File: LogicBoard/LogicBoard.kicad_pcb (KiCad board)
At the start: 4 copper layers, 80 x 81.5 mm, 54 parts, among them M1 MountingHole_3.5mm, M2 MountingHole_3.5mm, M3 MountingHole_3.5mm, M4 MountingHole_3.5mm, Q1 IRF520N, Q2 IRF520N, Q3 IRF520N, U1 STM32H743VITx, U2 MCP2557FD-xSN, U3 MCP2518FD-xQBB, U4 MCP2557FD-xSN, Y1 830033075, Y2 ABS04W32768KHZ6D2T5, Y3 ECS400936BCKYTR

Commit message: Added version with screw terminals
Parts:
- removed the C8 at (58.5, 96.0)
- added J**: TBC05041GG, TBC05-04-1-G-G:TBC05041GG, F.Cu at (45.0, 66.8)
- added J**: TBC05041GG, TBC05-04-1-G-G:TBC05041GG, F.Cu at (45.0, 80.0)
- added J**: TBC05041GG, TBC05-04-1-G-G:TBC05041GG, F.Cu at (46.0, 114.5)
- added MAIN ENCODERS: TBJ05081GG, TBJ05-08-1-G-G:TBJ05081GG, F.Cu at (57.4, 55.0)
- moved M4 12.5 mm to (44.0, 52.5)
- moved M3 11.5 mm to (116.0, 52.5)
- renumbered C5 to C1, C11 to C12, C5 to C2, C6 to C24
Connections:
- R10 pad 2: (no net) -> BatteryHealth
- R11 pad 2: (no net) -> BatteryHealth
- R12 pad 1: (no net) -> BatteryHealth
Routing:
- net TIM1_CH2: track 0.00 -> 53.2 mm, vias 0 -> 2
- net TIM1_CH1: track 0.00 -> 51.1 mm, vias 0 -> 2
- net I2C4_SDA: track 0.00 -> 48.3 mm, vias 0 -> 1
- net I2C2_SDA: track 0.00 -> 40.2 mm, vias 0 -> 2
- net TIM3_CH3: track 0.00 -> 40.1 mm, vias 0 -> 1
- net I2C2_SCL: track 0.00 -> 39.1 mm, vias 0 -> 2
- net TIM3_CH4: track 0.00 -> 38.0 mm, vias 0 -> 1
- net I2C3_SDA: track 0.00 -> 36.1 mm, vias 0 -> 2
- net TIM1_CH4: track 0.00 -> 36.0 mm
- net I2C4_SCL: track 0.00 -> 34.7 mm, vias 0 -> 1
- net TIM3_CH1: track 0.00 -> 34.7 mm
- net TIM1_CH3: track 0.00 -> 34.4 mm, vias 0 -> 1
- net TIM2_CH2: track 0.00 -> 32.9 mm, vias 0 -> 1
- net TIM3_CH2: track 0.00 -> 32.6 mm
- net I2C3_SCL: track 0.00 -> 32.4 mm, vias 0 -> 2
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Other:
- board size 80 x 81.5 mm -> 80.5 x 95 mm
- board text added: "G"
- board text added: "TIM1"
- board text added: "TIM2"
- board text added: "TIM3 (MOTORS)"

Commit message: Prepared BOM, component placement file and minor changes to PCB
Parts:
- C15: value C_0201_0603Metric -> C_0402; footprint Capacitor_SMD:C_0201_0603Metric -> PCM_4ms_Capacitor:C_0402
- J1: renamed from RPI CONN 
- J7: renamed from MAIN ENCODERS
- J8-STLINK: renamed from STLINK 
- R10, R11, R12: value R_0201_0603Metric -> R_1206_3216Metric; footprint Resistor_SMD:R_0201_0603Metric -> PCM_4ms_Resistor:R_1206_3216Metric
- Y1: value 830033075 -> 7I25000F18UCG
- Y3: value ECS400936BCKYTR -> Q24FA20H00209
- moved R11 6.66 mm to (49.1, 97.5)
- moved R10 6.50 mm to (53.0, 95.0), turned to 90 degrees
- moved R12 6.40 mm to (49.1, 94.5), turned to 0 degrees
- moved C15 0.50 mm to (57.0, 88.5)
- renumbered J** to J2, J** to J3, J** to J4, J** to J5, J** to J6
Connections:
- R11 pad 1: +24V -> BatteryHealth
- R11 pad 2: BatteryHealth -> +24V
- R12 pad 1: BatteryHealth -> GND
- R12 pad 2: GND -> BatteryHealth
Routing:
- net GND: track 90.5 -> 99.9 mm
- net BatteryHealth: track 12.7 -> 19.7 mm
- net +24V: track 49.7 -> 45.7 mm
- net VDDA_Conn: track 5.63 -> 5.04 mm

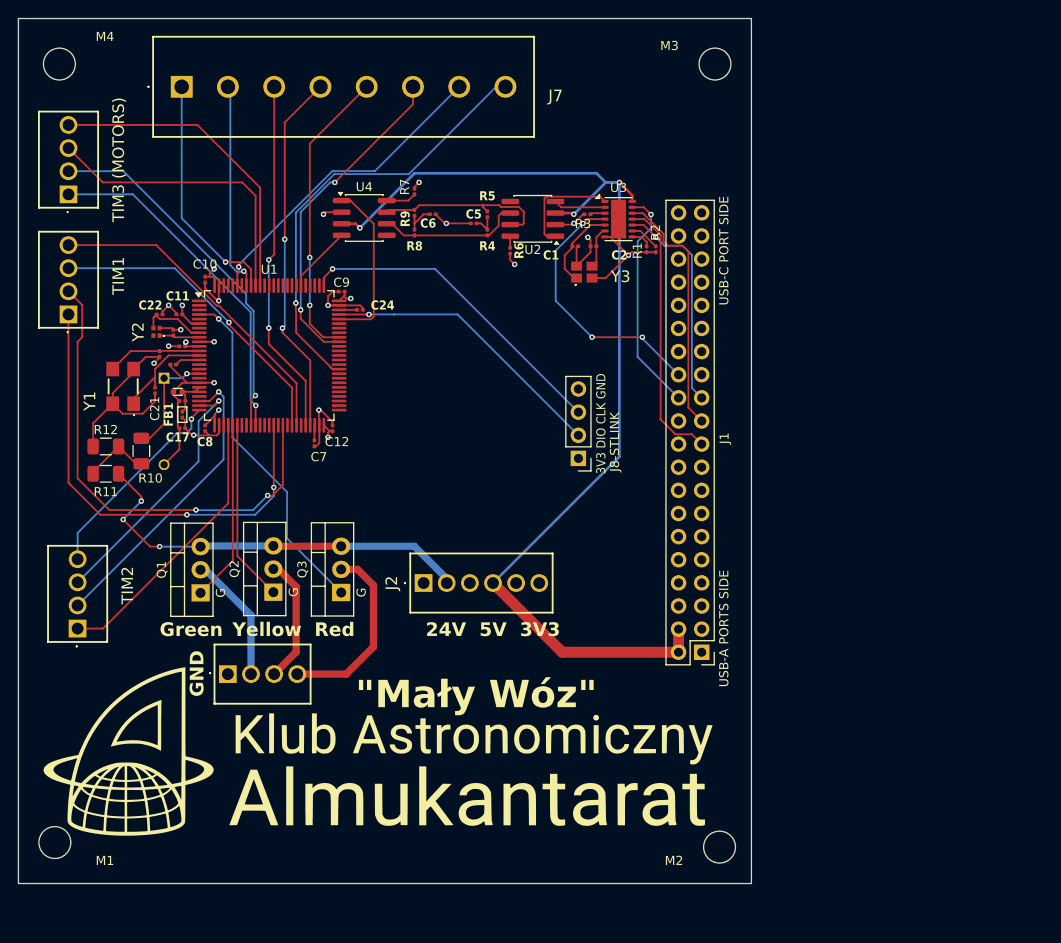
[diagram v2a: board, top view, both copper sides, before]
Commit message: PCB refactor, changed dimensions of passive components and board layout
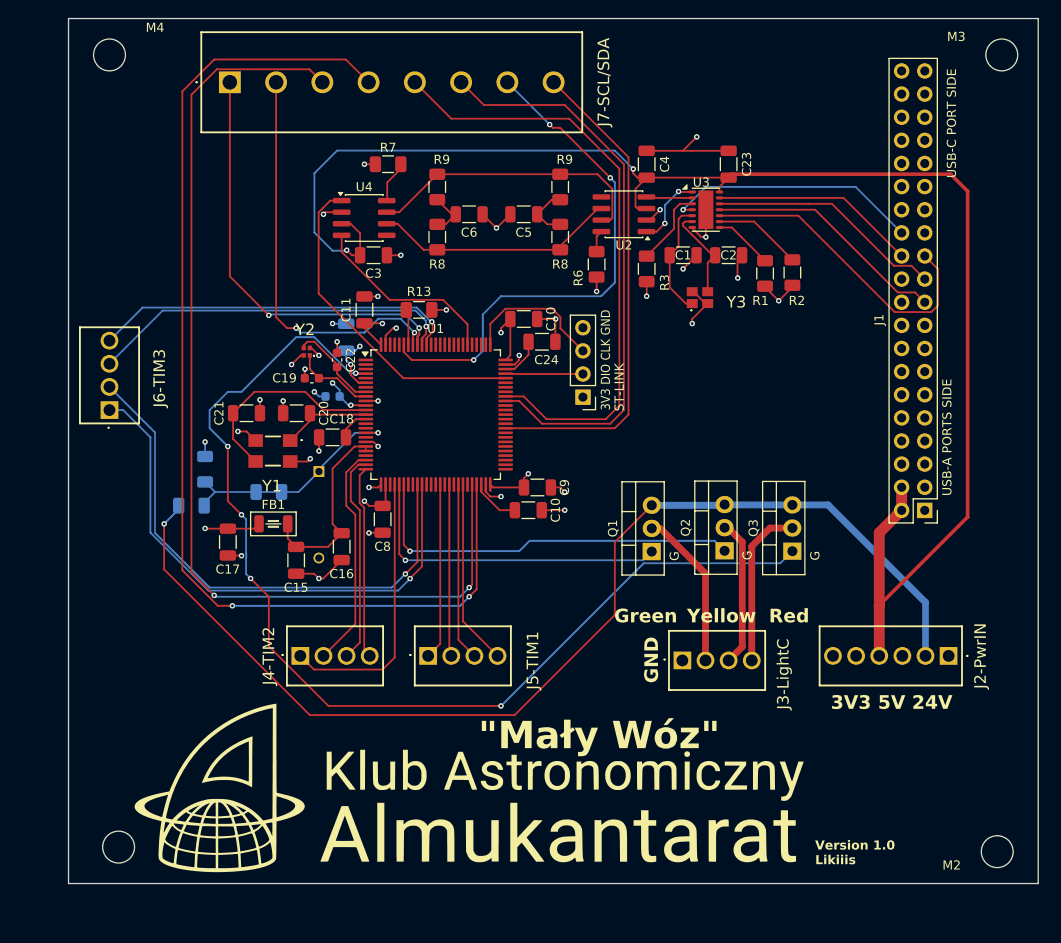
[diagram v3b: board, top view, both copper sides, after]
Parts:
- removed the C10 at (60.0, 76.2)
- removed the C12 at (57.5, 83.5)
- removed the C12 at (74.0, 92.5)
- removed the C21 at (54.5, 88.3)
- removed the C21 at (55.0, 84.3)
- removed C7: C_0201_0603Metric, Capacitor_SMD:C_0201_0603Metric
- removed R4, R5: R_0201_0603Metric, Resistor_SMD:R_0201_0603Metric
- removed the R8 at (83.0, 71.0)
- removed the R9 at (83.0, 68.8)
- added C10: C_1206_3216Metric, Capacitor_SMD:C_1206_3216Metric, F.Cu at (95.0, 80.5)
- added C10: C_1206_3216Metric, Capacitor_SMD:C_1206_3216Metric, F.Cu at (95.5, 101.5)
- added C12: C_1206_3216Metric, Capacitor_SMD:C_1206_3216Metric, B.Cu at (75.5, 82.5)
- added C13: C_0603_1608Metric, Capacitor_SMD:C_0603_1608Metric, B.Cu at (74.0, 89.0)
- added C20: C_1206_3216Metric, Capacitor_SMD:C_1206_3216Metric, F.Cu at (70.0, 90.8)
- added C21: C_1206_3216Metric, Capacitor_SMD:C_1206_3216Metric, F.Cu at (64.5, 90.8)
- added C23: C_1206_3216Metric, Capacitor_SMD:C_1206_3216Metric, F.Cu at (117.5, 63.5)
- added C3: C_1206_3216Metric, Capacitor_SMD:C_1206_3216Metric, F.Cu at (78.5, 73.5)
- added C4: C_1206_3216Metric, Capacitor_SMD:C_1206_3216Metric, F.Cu at (108.5, 63.5)
- added R13: R_1206_3216Metric, PCM_4ms_Resistor:R_1206_3216Metric, F.Cu at (83.5, 79.5)
- added R8: R_1206_3216Metric, PCM_4ms_Resistor:R_1206_3216Metric, F.Cu at (99.0, 71.5)
- added R8: R_1206_3216Metric, PCM_4ms_Resistor:R_1206_3216Metric, F.Cu at (85.5, 71.5)
- added R9: R_1206_3216Metric, PCM_4ms_Resistor:R_1206_3216Metric, F.Cu at (99.0, 66.0)
- added R9: R_1206_3216Metric, PCM_4ms_Resistor:R_1206_3216Metric, F.Cu at (85.5, 66.0)
- C1, C11, C16, C17, C18, C2, C24, C5, C6, C8, C9: value C_0201_0603Metric -> C_1206_3216Metric; footprint Capacitor_SMD:C_0201_0603Metric -> Capacitor_SMD:C_1206_3216Metric
- C15: value C_0402 -> C_1206_3216Metric; footprint PCM_4ms_Capacitor:C_0402 -> Capacitor_SMD:C_1206_3216Metric
- C19, C22: value C_0201_0603Metric -> C_0603_1608Metric; footprint Capacitor_SMD:C_0201_0603Metric -> Capacitor_SMD:C_0603_1608Metric
- FB1: value Ferrite_0201_0603Metric -> Ferrite_1206_3216Metric; footprint PCM_Ferrite_SMD_AKL:Ferrite_0201_0603Metric -> PCM_Ferrite_SMD_Handsoldering_AKL:Ferrite_1206_3216Metric
- R1, R2, R3, R6, R7: value R_0201_0603Metric -> R_1206_3216Metric; footprint Resistor_SMD:R_0201_0603Metric -> PCM_4ms_Resistor:R_1206_3216Metric
- R10, R11, R12: moved to B.Cu
- moved J2-PwrIN 58.2 mm to (141.7, 117.5), turned to 180 degrees
- moved J5-TIM1 54.5 mm to (84.5, 117.5), turned to 0 degrees
- moved J3-LightC 49.9 mm to (112.4, 118.0)
- moved Q2 49.8 mm to (117.1, 106.0)
- moved Q3 49.8 mm to (124.5, 106.0)
- moved Q1 49.8 mm to (109.1, 106.0)
- moved M3 31.5 mm to (147.5, 51.5)
- moved M2 30.5 mm to (147.0, 139.0)
- moved C9 30.4 mm to (96.5, 99.0), turned to 0 degrees
- moved J1 29.0 mm to (139.0, 101.5)
- moved J4-TIM2 24.6 mm to (70.5, 117.5), turned to 0 degrees
- moved J6-TIM3 24.1 mm to (49.5, 90.5)
- moved C16 23.7 mm to (75.0, 105.5), turned to -90 degrees
- moved C15 22.6 mm to (70.0, 107.0), turned to -90 degrees
- moved C8 21.9 mm to (79.5, 102.5)
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- renumbered J2 to J2-PwrIN, J3 to J3-LightC, J4 to J4-TIM2, J5 to J5-TIM1, J6 to J6-TIM3, J7 to J7-SCL/SDA, J8-STLINK to ST-LINK
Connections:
- C1 pad 1: Net-(C1--) -> GND
- C1 pad 2: GND -> Net-(C1--)
- C15 pad 1: GND -> VDDA_Conn
- C15 pad 2: VDDA_Conn -> GND
- C16 pad 1: GND -> VDDA_Conn
- C16 pad 2: VDDA_Conn -> GND
- C17 pad 1: GND -> +3V3
- C17 pad 2: +3V3 -> GND
- C18 pad 1: GND -> Net-(C18--)
- C18 pad 2: Net-(C18--) -> GND
- C19 pad 1: GND -> Net-(C19-+)
- C19 pad 2: Net-(C19-+) -> GND
- C2 pad 1: GND -> Net-(C2-+)
- C2 pad 2: Net-(C2-+) -> GND
- C22 pad 1: Net-(C22-+) -> GND
- C22 pad 2: GND -> Net-(C22-+)
- C24 pad 1: GND -> Net-(C24-+)
- C24 pad 2: Net-(C24-+) -> GND
- C5 pad 1: Cnn -> GND
- C5 pad 2: GND -> Cnn
- C6 pad 1: GND -> Cnn1
- C6 pad 2: Cnn -> GND
- C8 pad 1: GND -> +3V3
- C8 pad 2: +3V3 -> GND
- R1 pad 1: Net-(R1-+) -> GND
- R1 pad 2: GND -> Net-(R1-+)
- R2 pad 1: Net-(R2-+) -> GND
- R2 pad 2: GND -> Net-(R2-+)
- R3 pad 1: Net-(R3-+) -> GND
- R3 pad 2: GND -> Net-(R3-+)
- R6 pad 1: Net-(R6-+) -> GND
- R6 pad 2: GND -> Net-(R6-+)
- R7 pad 1: Net-(R7-+) -> GND
- R7 pad 2: GND -> Net-(R7-+)
- ST-LINK pad 1: +3V3 -> 3V3
- Y2 pad 4: (no net) -> GND
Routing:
- net I2C2_SDA: track 40.2 -> 121.7 mm
- net TIM15: track 37.9 -> 118.0 mm, vias 1 -> 5
- net +24V: track 45.7 -> 122.5 mm, vias 3 -> 1
- net I2C2_SCL: track 39.1 -> 112.1 mm
- net +5V: track 119.1 -> 168.8 mm, vias 3 -> 2
- net TIM1_CH2: track 53.2 -> 18.9 mm, vias 2 -> 0
- net I2C3_SCL: track 32.4 -> 66.6 mm, vias 2 -> 0
- net TIM1_CH1: track 51.1 -> 19.4 mm, vias 2 -> 0
- net I2C3_SDA: track 36.1 -> 63.3 mm, vias 2 -> 0
- net DEBUG_SWDIO: track 31.8 -> 8.52 mm, vias 1 -> 0
- net TIM14: track 20.0 -> 43.1 mm, vias 0 -> 1
- net I2C4_SCL: track 34.7 -> 57.6 mm, vias 1 -> 3
- net I2C1_SDA: track 23.2 -> 44.4 mm, vias 1 -> 2
- net TIM3_CH4: track 38.0 -> 58.8 mm
- net I2C1_SCL: track 26.2 -> 46.8 mm, vias 1 -> 2
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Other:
- board size 80.5 x 95 mm -> 106.5 x 95 mm
- board text added: "3V3 5V 24V"
- board text added: "Version 1.0 Likiiis"
- board text removed: "24V 5V 3V3"
- board text removed: "TIM1"
- board text removed: "TIM2"
- board text removed: "TIM3 (MOTORS)"

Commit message: Fix on LightColumn, added reverse-polarity protection, improved connectors, additional filtering lanes
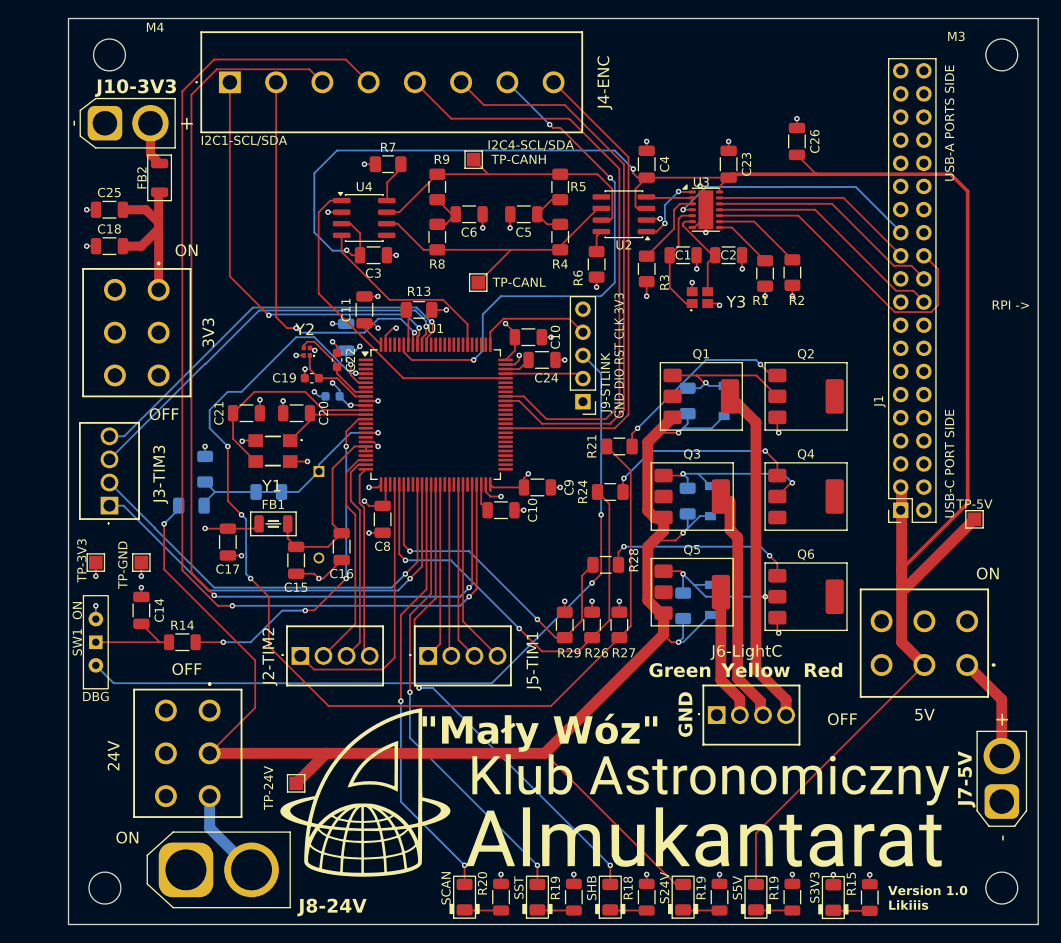
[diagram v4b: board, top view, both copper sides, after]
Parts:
- removed J2-PwrIN: TBC05061GG, TBC05-06-1-G-G:TBC05061GG
- removed ST-LINK: PINHD_1x4_Male, Connector_PinHeader_2.54mm:PinHeader_1x04_P2.54mm_Vertical
- added 24V: CS22BNW03, CS22BNW03:CS22BNW03, F.Cu at (60.5, 123.5)
- added 3V3: CS22BNW03, CS22BNW03:CS22BNW03, F.Cu at (54.9, 77.3)
- added 5V: CS22BNW03, CS22BNW03:CS22BNW03, F.Cu at (143.7, 118.5)
- added C14: C_1206_3216Metric, Capacitor_SMD:C_1206_3216Metric, F.Cu at (53.0, 112.5)
- added C25: C_1206_3216Metric, Capacitor_SMD:C_1206_3216Metric, F.Cu at (49.5, 68.5)
- added C26: C_1206_3216Metric, Capacitor_SMD:C_1206_3216Metric, F.Cu at (125.0, 61.0)
- added D2: ?, PCM_4ms_Diode:D_SOD-123, B.Cu at (115.5, 100.5)
- added D3: D3, PCM_4ms_Diode:D_SOD-123, B.Cu at (117.0, 89.5)
- added D4: ?, PCM_4ms_Diode:D_SOD-123, B.Cu at (115.5, 111.3)
- added FB2: Ferrite_1206_3216Metric, PCM_Ferrite_SMD_AKL:Ferrite_1206_3216Metric, F.Cu at (55.0, 65.0)
- added J10-3V3: AMASS_XT30U-F_1x02_P5.0mm_Vertical, Connector_AMASS:AMASS_XT30U-F_1x02_P5.0mm_Vertical, F.Cu at (49.0, 59.0)
- added J7-5V: AMASS_XT30U-F_1x02_P5.0mm_Vertical, Connector_AMASS:AMASS_XT30U-F_1x02_P5.0mm_Vertical, F.Cu at (147.5, 133.5)
- added J8-24V: AMASS_XT60-F_1x02_P7.20mm_Vertical, Connector_AMASS:AMASS_XT60-F_1x02_P7.20mm_Vertical, F.Cu at (57.9, 141.0)
- added J9-STLINK: PINHD_1x5_Male, Connector_PinHeader_2.54mm:PinHeader_1x05_P2.54mm_Vertical, F.Cu at (101.5, 89.6)
- added Q4: SOT-223, PCM_Package_TO_SOT_SMD_AKL:SOT-223, F.Cu at (126.0, 100.0)
- added Q5: SOT-223, PCM_Package_TO_SOT_SMD_AKL:SOT-223, F.Cu at (113.5, 110.5)
- added Q6: SOT-223, PCM_Package_TO_SOT_SMD_AKL:SOT-223, F.Cu at (126.0, 111.0)
- added R14: R_1206_3216Metric, Resistor_SMD:R_1206_3216Metric, F.Cu at (57.5, 116.0)
- added R15: R_1206_3216Metric, Resistor_SMD:R_1206_3216Metric, F.Cu at (133.0, 144.0)
- added R18: R_1206_3216Metric, Resistor_SMD:R_1206_3216Metric, F.Cu at (108.5, 144.0)
- added R19: R_1206_3216Metric, Resistor_SMD:R_1206_3216Metric, F.Cu at (124.5, 144.0)
- added R19: R_1206_3216Metric, Resistor_SMD:R_1206_3216Metric, F.Cu at (116.5, 144.0)
- added R19: R_1206_3216Metric, Resistor_SMD:R_1206_3216Metric, F.Cu at (100.5, 144.0)
- added R20: R_1206_3216Metric, Resistor_SMD:R_1206_3216Metric, F.Cu at (92.5, 144.0)
- added R21: R_1206_3216Metric, PCM_4ms_Resistor:R_1206_3216Metric, F.Cu at (105.5, 94.5)
- added R22: R_1206_3216Metric, PCM_4ms_Resistor:R_1206_3216Metric, B.Cu at (113.0, 89.5)
- added R23: R_1206_3216Metric, PCM_4ms_Resistor:R_1206_3216Metric, B.Cu at (112.5, 112.0)
- added R24: R_1206_3216Metric, PCM_4ms_Resistor:R_1206_3216Metric, F.Cu at (104.5, 99.5)
- added R25: R_1206_3216Metric, PCM_4ms_Resistor:R_1206_3216Metric, B.Cu at (113.0, 100.5)
- added R26: R_1206_3216Metric, PCM_4ms_Resistor:R_1206_3216Metric, F.Cu at (102.5, 114.1)
- added R27: R_1206_3216Metric, PCM_4ms_Resistor:R_1206_3216Metric, F.Cu at (105.5, 114.1)
- added R28: R_1206_3216Metric, PCM_4ms_Resistor:R_1206_3216Metric, F.Cu at (104.0, 107.5)
- added R29: R_1206_3216Metric, PCM_4ms_Resistor:R_1206_3216Metric, F.Cu at (99.5, 114.1)
- added S24V: LED_1206, PCM_LED_SMD_AKL:LED_1206_3216Metric, F.Cu at (112.5, 144.0)
- added S3V3: LED_1206, PCM_LED_SMD_AKL:LED_1206_3216Metric, F.Cu at (129.0, 144.0)
- added S5V: LED_1206, PCM_LED_SMD_AKL:LED_1206_3216Metric, F.Cu at (120.5, 144.0)
- added SCAN: LED_1206, PCM_LED_SMD_AKL:LED_1206_3216Metric, F.Cu at (88.5, 144.0)
- added SHB: LED_1206, PCM_LED_SMD_AKL:LED_1206_3216Metric, F.Cu at (104.5, 144.0)
- added SST: LED_1206, PCM_LED_SMD_AKL:LED_1206_3216Metric, F.Cu at (96.5, 144.0)
- added SW1: SW_Wuerth_450301014042, Button_Switch_THT:SW_Slide-03_Wuerth-WS-SLTV_10x2.5x6.4_P2.54mm, F.Cu at (48.0, 116.0)
- added TP-24V: TestPoint_Pad_1.5x1.5mm, TestPoint:TestPoint_Pad_1.5x1.5mm, F.Cu at (70.0, 131.5)
- added TP-3V3: TestPoint_Pad_1.5x1.5mm, TestPoint:TestPoint_Pad_1.5x1.5mm, F.Cu at (48.0, 107.2)
- added TP-5V: TestPoint_Pad_1.5x1.5mm, TestPoint:TestPoint_Pad_1.5x1.5mm, F.Cu at (144.5, 102.5)
- added TP-CANH: TestPoint_Pad_1.5x1.5mm, TestPoint:TestPoint_Pad_1.5x1.5mm, F.Cu at (89.5, 63.0)
- added TP-CANL: TestPoint_Pad_1.5x1.5mm, TestPoint:TestPoint_Pad_1.5x1.5mm, F.Cu at (90.0, 76.5)
- added TP-GND: TestPoint_Pad_1.5x1.5mm, TestPoint:TestPoint_Pad_1.5x1.5mm, F.Cu at (53.0, 107.2)
- J1: value PinHeader_2x20_P2.54mm_Vertical -> PinSocket_2x20_P2.54mm_Vertical; footprint Connector_PinHeader_2.54mm:PinHeader_2x20_P2.54mm_Vertical -> Connector_PinSocket_2.54mm:PinSocket_2x20_P2.54mm_Vertical
- Q1, Q2, Q3: value IRF520N -> SOT-223; footprint PCM_Package_TO_SOT_THT_AKL:TO-220-3_Vertical_GDS -> PCM_Package_TO_SOT_SMD_AKL:SOT-223
- moved C18 32.3 mm to (49.5, 72.5), turned to 0 degrees
- moved Q2 19.2 mm to (126.0, 89.0), turned to 0 degrees
- moved Q1 17.9 mm to (114.5, 89.0), turned to 0 degrees
- moved G*** 16.0 mm to (105.0, 132.5)
- moved Q3 12.5 mm to (113.5, 100.0), turned to 0 degrees
- moved J3-TIM3 10.5 mm to (49.5, 101.0)
- moved J6-LightC 7.09 mm to (116.2, 124.0)
- moved M1 4.74 mm to (49.0, 143.0)
- moved M2 4.03 mm to (147.5, 143.0)
- moved C10 3.00 mm to (92.5, 101.5)
- moved J1 2.64 mm to (136.4, 101.5)
- moved C10 2.06 mm to (95.5, 82.5)
- moved C24 2.00 mm to (97.0, 85.0)
- renumbered J4-TIM2 to J2-TIM2, J6-TIM3 to J3-TIM3, J7-SCL/SDA to J4-ENC, J3-LightC to J6-LightC, R8 to R4, R9 to R5
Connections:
- C18 pad 1: Net-(C18--) -> GND
- C18 pad 2: GND -> +3V3
- J1 pad 1: (no net) -> +5V
- J1 pad 10: (no net) -> GND
- J1 pad 13: (no net) -> GND
- J1 pad 14: GND -> (no net)
- J1 pad 19: SPI1_SDI -> GND
- J1 pad 2: +5V -> (no net)
- J1 pad 20: GND -> SPI1_SDI
- J1 pad 21: SPI1_SDO -> (no net)
- J1 pad 22: (no net) -> SPI1_SDO
- J1 pad 23: SPI1_SCLK -> SPI1_CS
- J1 pad 24: SPI1_CS -> SPI1_SCLK
- J1 pad 25: GND -> SPI1_INT
- J1 pad 26: SPI1_INT -> GND
- J1 pad 29: (no net) -> GND
- J1 pad 3: (no net) -> +5V
- J1 pad 30: GND -> (no net)
- J1 pad 33: (no net) -> GND
- J1 pad 34: GND -> (no net)
- J1 pad 39: GND -> (no net)
- J1 pad 4: +5V -> (no net)
- J1 pad 40: (no net) -> GND
- J1 pad 5: (no net) -> GND
- J1 pad 6: GND -> (no net)
- J1 pad 9: GND -> (no net)
- Q1 pad 1: TIM13 -> Q1-Q2
- Q1 pad 2: GreenLight_Modulated -> (no net)
- Q2 pad 1: TIM14 -> TIM15
- Q2 pad 2: YellowLight_Modulated -> Q1-Q2
- Q2 pad 3: +24V -> GND
- Q3 pad 1: TIM15 -> Q3-Q4
- Q3 pad 2: RedLight_Modulated -> (no net)
- U1 pad 14: Net-(C18--) -> Net-(R14-+)
- U1 pad 36: unconnected-(U1-PB2-Pad36) -> CANActivity
- U1 pad 37: unconnected-(U1-PE7-Pad37) -> StatusLED
- U1 pad 38: unconnected-(U1-PE8-Pad38) -> HeartBeat
- U2 pad 6: Net-(R4--) -> CanL
- U2 pad 7: Net-(R5-+) -> CanH
- U4 pad 6: Net-(R4--) -> CanL
- U4 pad 7: Net-(R5-+) -> CanH
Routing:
- net DEBUG_RST: track 0.00 -> 86.6 mm, vias 0 -> 2
- net +24V: track 122.5 -> 182.7 mm, vias 1 -> 4
- net HeartBeat: track 0.00 -> 54.7 mm, vias 0 -> 2
- net +5V: track 168.8 -> 222.3 mm
- net StatusLED: track 0.00 -> 50.7 mm, vias 0 -> 2
- net CANActivity: track 0.00 -> 48.0 mm, vias 0 -> 2
- net Net-(R14-+): track 0.00 -> 38.3 mm, vias 0 -> 4
- net TIM13: track 36.1 -> 72.8 mm, vias 1 -> 4
- net +3V3: track 39.8 -> 68.3 mm, vias 9 -> 12
- net TIM15: track 118.0 -> 139.1 mm, vias 5 -> 6
- net Q3-Q4: track 0.00 -> 20.6 mm, vias 0 -> 2
- net RedLight_Modulated: track 17.8 -> 37.6 mm
- net Q1-Q2: track 0.00 -> 18.2 mm, vias 0 -> 1
- net Q5-Q6: track 0.00 -> 17.6 mm, vias 0 -> 2
- net TIM14: track 43.1 -> 59.0 mm, vias 1 -> 4
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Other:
- board size 106.5 x 95 mm -> 106.5 x 99.5 mm
- board text added: "DBG"
- board text added: "GND DIO RST CLK 3V3"
- board text added: "I2C1-SCL/SDA"
- board text added: "I2C4-SCL/SDA"
- board text added: "OFF"
- board text added: "ON"
- board text added: "RPI ->"
- board text removed: "3V3 5V 24V"
- board text removed: "3V3 DIO CLK GND"
- board text removed: "G"

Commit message: Fixes to tags, nets and silkscreen
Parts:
- removed C13: C_0603_1608Metric, Capacitor_SMD:C_0603_1608Metric
- added C20: C_1206_3216Metric, Capacitor_SMD:C_1206_3216Metric, F.Cu at (71.5, 88.0)
- moved C19 1.24 mm to (71.0, 86.0)
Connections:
- R4 pad 1: Net-(R4--) -> CanL
- R5 pad 2: Net-(R5-+) -> CanH
- R8 pad 1: Net-(R4--) -> CanL
- R9 pad 2: Net-(R5-+) -> CanH
- TP-CANH pad 1: Net-(R5-+) -> CanH
- TP-CANL pad 1: Net-(R4--) -> CanL
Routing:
- net Net-(R5-+): track 33.9 -> 0.00 mm
- net CanH: track 0.00 -> 33.9 mm
- net Net-(R4--): track 32.0 -> 0.00 mm
- net CanL: track 0.00 -> 32.0 mm
- net GND: track 90.1 -> 95.1 mm, vias 60 -> 61
- net +3V3: track 68.3 -> 71.1 mm, vias 12 -> 11
- net TIM15: track 139.1 -> 140.0 mm
- net Net-(C21-+): track 22.7 -> 21.9 mm

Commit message: Removed power switches
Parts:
- removed 24V, 3V3, 5V: CS22BNW03, CS22BNW03:CS22BNW03
- moved TP-5V 7.43 mm to (149.5, 108.0)
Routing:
- net +5V: track 222.3 -> 231.4 mm
- net +24V: track 182.7 -> 177.7 mm
- net +3V3: track 71.1 -> 67.3 mm, vias 11 -> 12
- net BatteryHealth: track 26.1 -> 23.1 mm
